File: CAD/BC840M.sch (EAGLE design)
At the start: 87 parts, among them J1 SM02B-SRSS-TB(LF)(SN), U2 BC840M, U3 LP5907MFX-3.3/NOPB, U4 LP5907MFX-3.3/NOPB, U5 ADS131M08IPBS, X1 ABM3B-8.000MHZ-B2-T, X2 FC-12M

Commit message: tweaks
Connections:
- new net VDDH: R2.2, R25.1, R28.1, R29.1, U2.A7/VDDH
- net VDD: no longer R2.2, R25.1, R28.1, R29.1, U2.A7/VDDH
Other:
- moved on the sheet: R30, R31

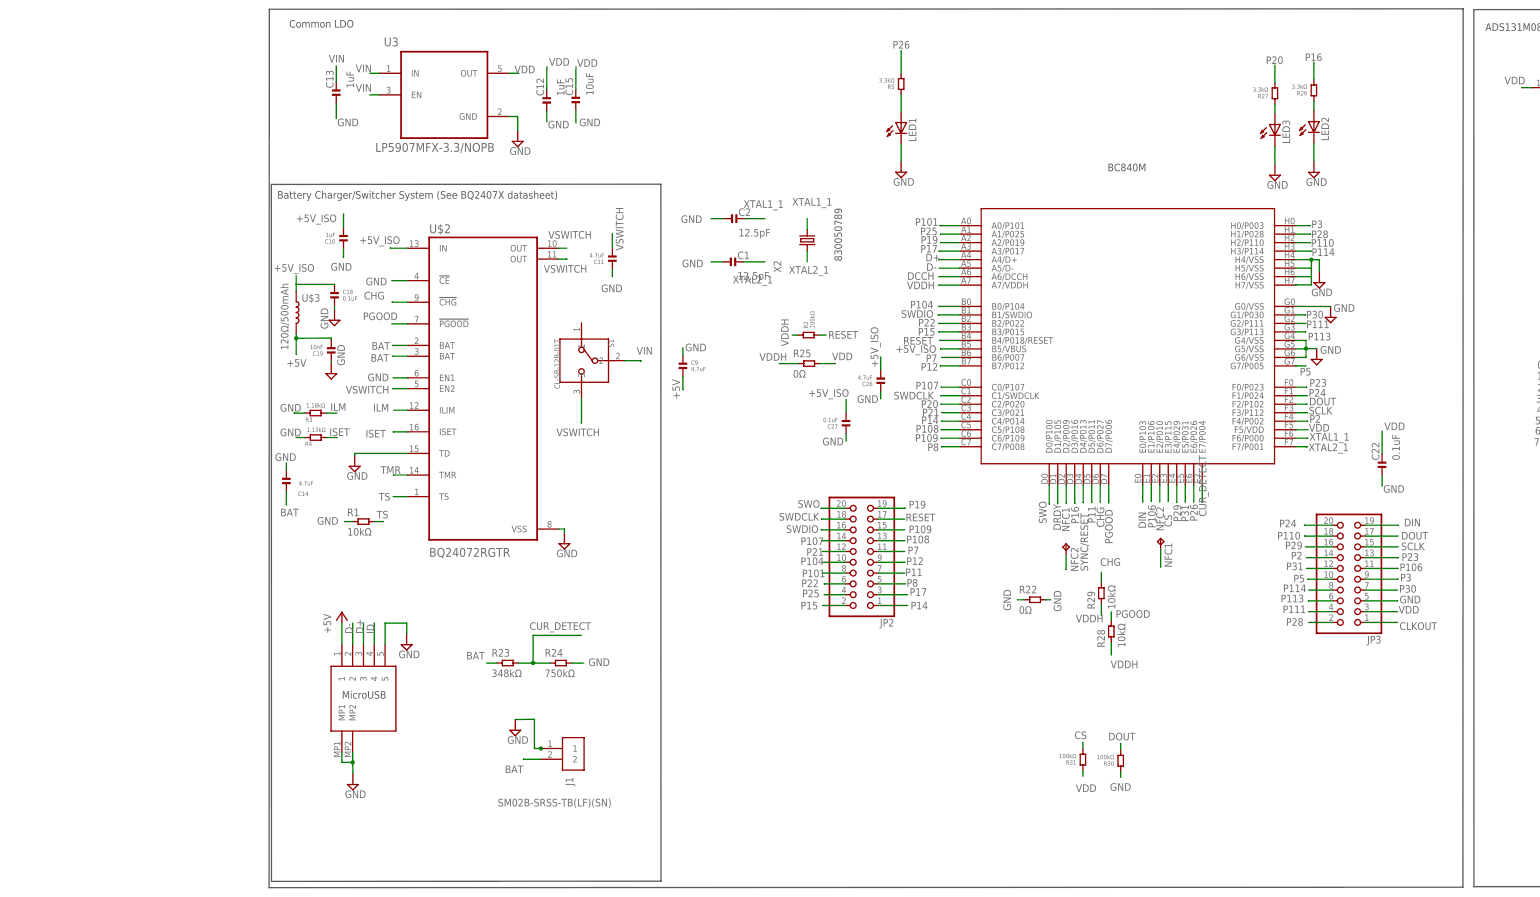
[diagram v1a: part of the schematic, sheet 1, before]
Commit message: added TVS diodes
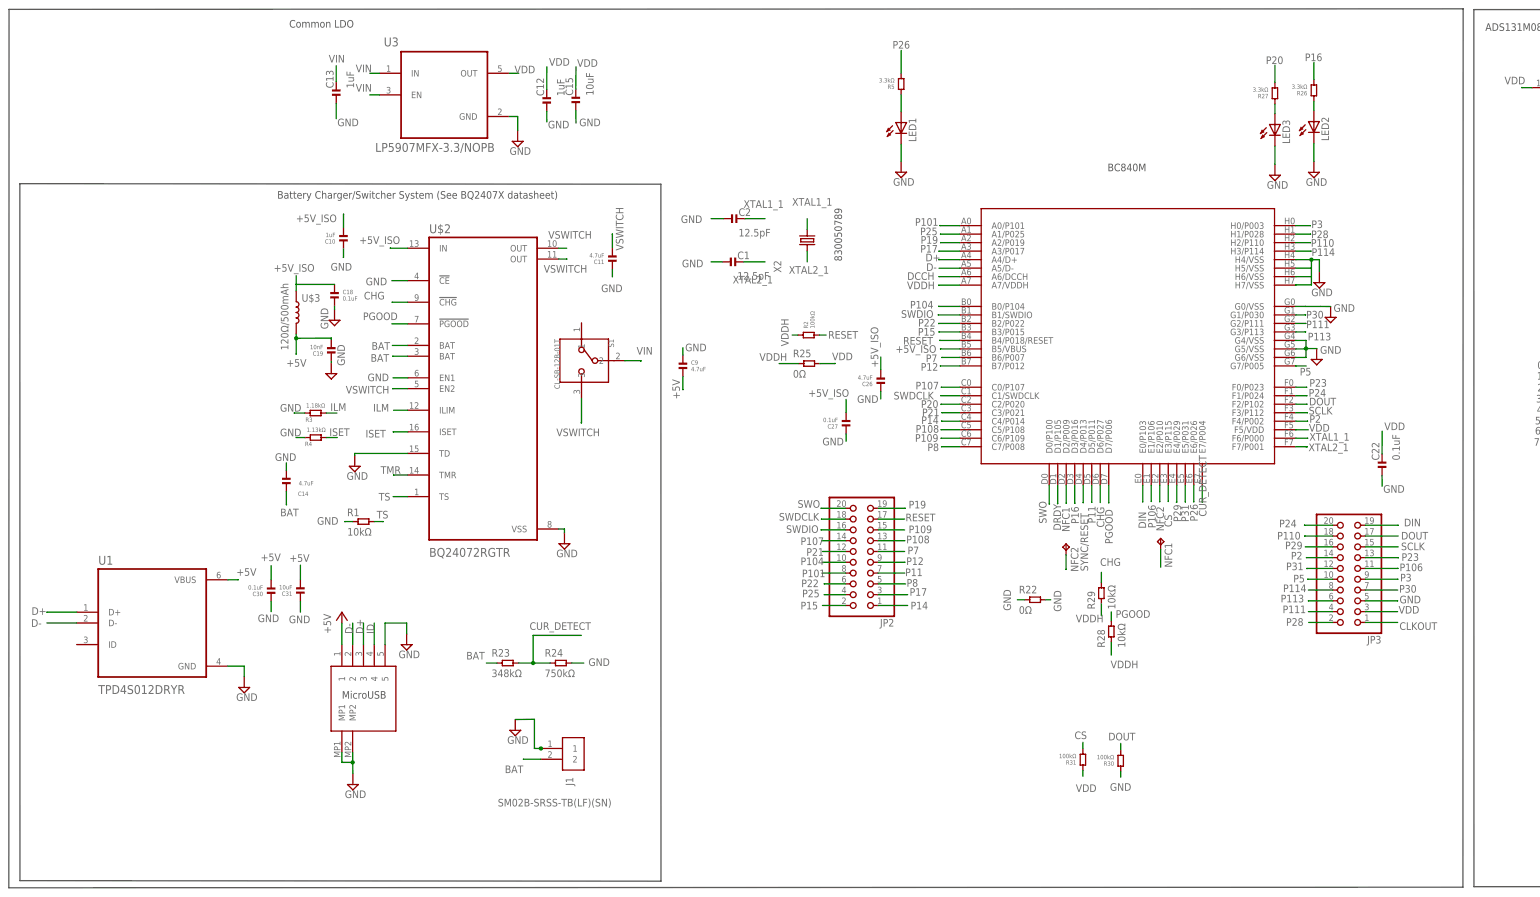
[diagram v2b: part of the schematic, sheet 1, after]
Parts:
- added C30: 0.1uF, standardparts:CAPACITOR.0201
- added C31: 10uF, standardparts:CAPACITOR.0201
- added U1: TPD4S012DRYR, TPD4S012DRYR:TPD4S012DRYR
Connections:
- net +5V: now also C30.2, C31.2, U1.VBUS
- net D+: now also U1.D+
- net D-: now also U1.D-
- net GND: now also C30.1, C31.1, U1.GND
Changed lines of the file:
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@@
 <part name="R30" library="standardparts" deviceset="RESISTOR" device=".0402" value="100kΩ"/>
 <part name="R31" library="standardparts" deviceset="RESISTOR" device=".0402" value="100kΩ"/>
+<part name="U1" library="TPD4S012DRYR" deviceset="TPD4S012DRYR" device=""/>
+<part name="SUPPLY10" library="supply2" library_urn="urn:adsk.eagle:library:372" deviceset="GND" device=""/>
+<part name="C30" library="standardparts" deviceset="CAPACITOR" device=".0201" value="0.1uF"/>
+<part name="C31" library="standardparts" deviceset="CAPACITOR" device=".0201" value="10uF"/>
 </parts>
 <sheets>
@@
 <text x="35.179" y="50.9016" size="1.778" layer="97">MicroUSB</text>
 <wire x1="110.236" y1="7.9756" x2="110.2106" y2="171.9072" width="0.1524" layer="97"/>
-<wire x1="110.2106" y1="171.9072" x2="18.5928" y2="171.8564" width="0.1524" layer="97"/>
-<wire x1="18.5928" y1="171.8564" x2="18.6182" y2="7.9248" width="0.1524" layer="97"/>
-<wire x1="18.6182" y1="7.9248" x2="110.236" y2="7.9756" width="0.1524" layer="97"/>
+<wire x1="110.2106" y1="171.9072" x2="-40.5638" y2="172.0342" width="0.1524" layer="97"/>
+<wire x1="-40.5638" y1="172.0342" x2="-40.5384" y2="8.1026" width="0.1524" layer="97"/>
+<wire x1="-40.5384" y1="8.1026" x2="110.236" y2="7.9756" width="0.1524" layer="97"/>
 <text x="19.9644" y="168.5036" size="1.778" layer="97">Battery Charger/Switcher System (See BQ2407X datasheet)</text>
 <wire x1="476.7072" y1="6.6802" x2="301.4472" y2="6.6802" width="0.1524" layer="97"/>
@@
 <wire x1="476.6818" y1="212.979" x2="476.7072" y2="6.6802" width="0.1524" layer="97"/>
 <text x="304.1142" y="207.9752" size="1.778" layer="97">ADS131M08 Circuitry</text>
-<wire x1="18.1102" y1="213.0552" x2="298.9072" y2="213.1568" width="0.1524" layer="97"/>
+<wire x1="-43.1038" y1="213.0298" x2="298.9072" y2="213.1568" width="0.1524" layer="97"/>
 <wire x1="298.9072" y1="213.1568" x2="298.8564" y2="6.5532" width="0.1524" layer="97"/>
-<wire x1="298.8564" y1="6.5532" x2="18.0594" y2="6.4516" width="0.1524" layer="97"/>
-<wire x1="18.0594" y1="6.4516" x2="18.1102" y2="213.0552" width="0.1524" layer="97"/>
+<wire x1="298.8564" y1="6.5532" x2="-43.1546" y2="6.4262" width="0.1524" layer="97"/>
+<wire x1="-43.1546" y1="6.4262" x2="-43.1038" y2="213.0298" width="0.1524" layer="97"/>
 <text x="22.7838" y="208.7372" size="1.778" layer="97">Common LDO</text>
 <text x="215.265" y="174.9552" size="1.778" layer="97">BC840M</text>
@@
 <attribute name="NAME" x="207.9244" y="35.3822" size="1.016" layer="95" rot="MR0"/>
 <attribute name="VALUE" x="207.9244" y="37.9222" size="1.016" layer="96" rot="R180"/>
+</instance>
+<instance part="U1" gate="G$1" x="-9.4234" y="68.707" smashed="yes">
+<attribute name="NAME" x="-22.1234" y="82.407" size="2.0828" layer="95" ratio="10" rot="SR0"/>
+<attribute name="VALUE" x="-22.1234" y="52.007" size="2.0828" layer="96" ratio="10" rot="SR0"/>
+</instance>
+<instance part="SUPPLY10" gate="GND" x="12.2174" y="53.5432" smashed="yes">
+<attribute name="VALUE" x="10.3124" y="50.3682" size="1.778" layer="96"/>
+</instance>
+<instance part="C30" gate="G$1" x="18.542" y="76.3016" smashed="yes" rot="R90">
+<attribute name="NAME" x="16.637" y="75.0316" size="1.016" layer="95" rot="MR0"/>
+<attribute name="VALUE" x="16.637" y="77.5716" size="1.016" layer="96" rot="R180"/>
+</instance>
+<instance part="C31" gate="G$1" x="25.4254" y="76.3524" smashed="yes" rot="R90">
+<attribute name="NAME" x="23.5204" y="75.0824" size="1.016" layer="95" rot="MR0"/>
+<attribute name="VALUE" x="23.5204" y="77.6224" size="1.016" layer="96" rot="R180"/>
 </instance>
 </instances>
@@
 <label x="215.8238" y="29.2354" size="1.778" layer="95"/>
 </segment>
+<segment>
+<pinref part="U1" gate="G$1" pin="GND"/>
+<pinref part="SUPPLY10" gate="GND" pin="GND"/>
+<wire x1="8.3566" y1="58.547" x2="12.2174" y2="58.547" width="0.1524" layer="91"/>
+<wire x1="12.2174" y1="58.547" x2="12.2174" y2="56.0832" width="0.1524" layer="91"/>
+</segment>
+<segment>
+<pinref part="C30" gate="G$1" pin="1"/>
+<wire x1="18.542" y1="73.7616" x2="18.542" y2="71.374" width="0.1524" layer="91"/>
+<label x="15.3924" y="68.9102" size="1.778" layer="95"/>
+</segment>
+<segment>
+<pinref part="C31" gate="G$1" pin="1"/>
+<wire x1="25.4254" y1="73.8124" x2="25.4254" y2="71.247" width="0.1524" layer="91"/>
+<label x="22.7076" y="68.6562" size="1.778" layer="95"/>
+</segment>
 </net>
 <net name="CLKIN" class="0">
@@
 <label x="114.681" y="121.3104" size="1.778" layer="95" rot="R90"/>
 </segment>
+<segment>
+<pinref part="U1" gate="G$1" pin="VBUS"/>
+<wire x1="8.3566" y1="78.867" x2="10.7696" y2="78.867" width="0.1524" layer="91"/>
+<wire x1="10.7696" y1="78.867" x2="10.7696" y2="78.8924" width="0.1524" layer="91"/>
+<label x="10.3632" y="79.8068" size="1.778" layer="95"/>
+</segment>
+<segment>
+<pinref part="C30" gate="G$1" pin="2"/>
+<wire x1="18.542" y1="78.8416" x2="18.542" y2="82.1944" width="0.1524" layer="91"/>
+<label x="16.0782" y="83.2612" size="1.778" layer="95"/>
+</segment>
+<segment>
+<pinref part="C31" gate="G$1" pin="2"/>
+<wire x1="25.4254" y1="78.8924" x2="25.4254" y2="82.3214" width="0.1524" layer="91"/>
+<label x="22.8346" y="83.0834" size="1.778" layer="95"/>
+</segment>
 </net>
 <net name="D-" class="0">
@@
 <label x="172.6184" y="151.511" size="1.778" layer="95"/>
 </segment>
+<segment>
+<pinref part="U1" gate="G$1" pin="D-"/>
+<wire x1="-27.2034" y1="68.707" x2="-34.1884" y2="68.707" width="0.1524" layer="91"/>
+<label x="-37.9222" y="67.7926" size="1.778" layer="95"/>
+</segment>
 </net>
 <net name="D+" class="0">
@@
 <label x="172.4406" y="153.7716" size="1.778" layer="95"/>
 </segment>
-</net>
+<segment>
+<pinref part="U1" gate="G$1" pin="D+"/>
+<wire x1="-27.2034" y1="71.247" x2="-34.1884" y2="71.247" width="0.1524" layer="91"/>
+<wire x1="-34.1884" y1="71.247" x2="-34.1884" y2="71.2216" width="0.1524" layer="91"/>
+<label x="-37.8206" y="70.612" size="1.778" layer="95"/>
+</segment>
+</net>

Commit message: push
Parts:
- C16, C17, C20, C21, C24, C25, C28, C29: value 10pF -> 100pF
- R10, R11, R12, R13, R14, R15, R16, R17, R18, R19, R20, R21, R6, R7, R8, R9: value 10MOhm -> 1MOhm
- renumbered U$1 to U7, U$2 to U6, U$3 to I1

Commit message: latest
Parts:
- C15, C31: device standardparts:CAPACITOR.0201 -> standardparts:CAPACITOR.0402
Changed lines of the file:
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@@
 <grid distance="1" unitdist="mil" unit="mil" style="lines" multiple="1" display="no" altdistance="0.01" altunitdist="inch" altunit="inch"/>
 <layers>
-<layer number="1" name="Top" color="4" fill="1" visible="no" active="no"/>
-<layer number="2" name="Route2" color="16" fill="1" visible="no" active="no"/>
-<layer number="3" name="Route3" color="17" fill="1" visible="no" active="no"/>
-<layer number="4" name="Route4" color="18" fill="1" visible="no" active="no"/>
-<layer number="5" name="Route5" color="19" fill="1" visible="no" active="no"/>
-<layer number="6" name="Route6" color="25" fill="1" visible="no" active="no"/>
-<layer number="7" name="Route7" color="26" fill="1" visible="no" active="no"/>
-<layer number="8" name="Route8" color="27" fill="1" visible="no" active="no"/>
-<layer number="9" name="Route9" color="28" fill="1" visible="no" active="no"/>
-<layer number="10" name="Route10" color="29" fill="1" visible="no" active="no"/>
-<layer number="11" name="Route11" color="30" fill="1" visible="no" active="no"/>
-<layer number="12" name="Route12" color="20" fill="1" visible="no" active="no"/>
-<layer number="13" name="Route13" color="21" fill="1" visible="no" active="no"/>
-<layer number="14" name="Route14" color="22" fill="1" visible="no" active="no"/>
-<layer number="15" name="Route15" color="23" fill="1" visible="no" active="no"/>
-<layer number="16" name="Bottom" color="1" fill="1" visible="no" active="no"/>
-<layer number="17" name="Pads" color="2" fill="1" visible="no" active="no"/>
-<layer number="18" name="Vias" color="2" fill="1" visible="no" active="no"/>
-<layer number="19" name="Unrouted" color="6" fill="1" visible="no" active="no"/>
-<layer number="20" name="Dimension" color="24" fill="1" visible="no" active="no"/>
-<layer number="21" name="tPlace" color="7" fill="1" visible="no" active="no"/>
-<layer number="22" name="bPlace" color="7" fill="1" visible="no" active="no"/>
-<layer number="23" name="tOrigins" color="15" fill="1" visible="no" active="no"/>
-<layer number="24" name="bOrigins" color="15" fill="1" visible="no" active="no"/>
-<layer number="25" name="tNames" color="7" fill="1" visible="no" active="no"/>
-<layer number="26" name="bNames" color="7" fill="1" visible="no" active="no"/>
-<layer number="27" name="tValues" color="7" fill="1" visible="no" active="no"/>
-<layer number="28" name="bValues" color="7" fill="1" visible="no" active="no"/>
+<layer number="1" name="Top" color="4" fill="1" visible="yes" active="no"/>
+<layer number="2" name="Route2" color="16" fill="1" visible="yes" active="no"/>
+<layer number="3" name="Route3" color="17" fill="1" visible="yes" active="no"/>
+<layer number="4" name="Route4" color="18" fill="1" visible="yes" active="no"/>
+<layer number="5" name="Route5" color="19" fill="1" visible="yes" active="no"/>
+<layer number="6" name="Route6" color="25" fill="1" visible="yes" active="no"/>
+<layer number="7" name="Route7" color="26" fill="1" visible="yes" active="no"/>
+<layer number="8" name="Route8" color="27" fill="1" visible="yes" active="no"/>
+<layer number="9" name="Route9" color="28" fill="1" visible="yes" active="no"/>
+<layer number="10" name="Route10" color="29" fill="1" visible="yes" active="no"/>
+<layer number="11" name="Route11" color="30" fill="1" visible="yes" active="no"/>
+<layer number="12" name="Route12" color="20" fill="1" visible="yes" active="no"/>
+<layer number="13" name="Route13" color="21" fill="1" visible="yes" active="no"/>
+<layer number="14" name="Route14" color="22" fill="1" visible="yes" active="no"/>
+<layer number="15" name="Route15" color="23" fill="1" visible="yes" active="no"/>
+<layer number="16" name="Bottom" color="1" fill="1" visible="yes" active="no"/>
+<layer number="17" name="Pads" color="2" fill="1" visible="yes" active="no"/>
+<layer number="18" name="Vias" color="2" fill="1" visible="yes" active="no"/>
+<layer number="19" name="Unrouted" color="6" fill="1" visible="yes" active="no"/>
+<layer number="20" name="Dimension" color="24" fill="1" visible="yes" active="no"/>
+<layer number="21" name="tPlace" color="7" fill="1" visible="yes" active="no"/>
+<layer number="22" name="bPlace" color="7" fill="1" visible="yes" active="no"/>
+<layer number="23" name="tOrigins" color="15" fill="1" visible="yes" active="no"/>
+<layer number="24" name="bOrigins" color="15" fill="1" visible="yes" active="no"/>
+<layer number="25" name="tNames" color="7" fill="1" visible="yes" active="no"/>
+<layer number="26" name="bNames" color="7" fill="1" visible="yes" active="no"/>
+<layer number="27" name="tValues" color="7" fill="1" visible="yes" active="no"/>
+<layer number="28" name="bValues" color="7" fill="1" visible="yes" active="no"/>
 <layer number="29" name="tStop" color="7" fill="3" visible="no" active="no"/>
 <layer number="30" name="bStop" color="7" fill="6" visible="no" active="no"/>
@@
 <layer number="35" name="tGlue" color="7" fill="4" visible="no" active="no"/>
 <layer number="36" name="bGlue" color="7" fill="5" visible="no" active="no"/>
-<layer number="37" name="tTest" color="7" fill="1" visible="no" active="no"/>
-<layer number="38" name="bTest" color="7" fill="1" visible="no" active="no"/>
+<layer number="37" name="tTest" color="7" fill="1" visible="yes" active="no"/>
+<layer number="38" name="bTest" color="7" fill="1" visible="yes" active="no"/>
 <layer number="39" name="tKeepout" color="4" fill="11" visible="no" active="no"/>
 <layer number="40" name="bKeepout" color="1" fill="11" visible="no" active="no"/>
@@
 <layer number="44" name="Drills" color="7" fill="1" visible="no" active="no"/>
 <layer number="45" name="Holes" color="7" fill="1" visible="no" active="no"/>
-<layer number="46" name="Milling" color="3" fill="1" visible="no" active="no"/>
-<layer number="47" name="Measures" color="7" fill="1" visible="no" active="no"/>
-<layer number="48" name="Document" color="7" fill="1" visible="no" active="no"/>
-<layer number="49" name="Reference" color="7" fill="1" visible="no" active="no"/>
-<layer number="50" name="dxf" color="7" fill="1" visible="no" active="no"/>
-<layer number="51" name="tDocu" color="7" fill="1" visible="no" active="no"/>
-<layer number="52" name="bDocu" color="7" fill="1" visible="no" active="no"/>
-<layer number="53" name="tGND_GNDA" color="7" fill="9" visible="no" active="no"/>
-<layer number="54" name="bGND_GNDA" color="1" fill="9" visible="no" active="no"/>
-<layer number="56" name="wert" color="7" fill="1" visible="no" active="no"/>
-<layer number="57" name="tCAD" color="7" fill="1" visible="no" active="no"/>
-<layer number="58" name="bCAD" color="7" fill="1" visible="no" active="no"/>
-<layer number="59" name="tCarbon" color="7" fill="1" visible="no" active="no"/>
-<layer number="60" name="bCarbon" color="7" fill="1" visible="no" active="no"/>
+<layer number="46" name="Milling" color="3" fill="1" visible="yes" active="no"/>
+<layer number="47" name="Measures" color="7" fill="1" visible="yes" active="no"/>
+<layer number="48" name="Document" color="7" fill="1" visible="yes" active="no"/>
+<layer number="49" name="Reference" color="7" fill="1" visible="yes" active="no"/>
+<layer number="50" name="dxf" color="7" fill="1" visible="yes" active="no"/>
+<layer number="51" name="tDocu" color="7" fill="1" visible="yes" active="no"/>
+<layer number="52" name="bDocu" color="7" fill="1" visible="yes" active="no"/>
+<layer number="53" name="tGND_GNDA" color="7" fill="9" visible="yes" active="no"/>
+<layer number="54" name="bGND_GNDA" color="1" fill="9" visible="yes" active="no"/>
+<layer number="56" name="wert" color="7" fill="1" visible="yes" active="no"/>
+<layer number="57" name="tCAD" color="7" fill="1" visible="yes" active="no"/>
+<layer number="58" name="bCAD" color="7" fill="1" visible="yes" active="no"/>
+<layer number="59" name="tCarbon" color="7" fill="1" visible="yes" active="no"/>
+<layer number="60" name="bCarbon" color="7" fill="1" visible="yes" active="no"/>
 <layer number="88" name="SimResults" color="9" fill="1" visible="yes" active="yes"/>
 <layer number="89" name="SimProbes" color="9" fill="1" visible="yes" active="yes"/>
@@
 <part name="SUPPLY7" library="supply2" library_urn="urn:adsk.eagle:library:372" deviceset="GND" device=""/>
 <part name="SUPPLY11" library="supply2" library_urn="urn:adsk.eagle:library:372" deviceset="GND" device=""/>
-<part name="C15" library="standardparts" deviceset="CAPACITOR" device=".0201" value="10uF"/>
+<part name="C15" library="standardparts" deviceset="CAPACITOR" device=".0402" value="10uF"/>
 <part name="SUPPLY13" library="supply2" library_urn="urn:adsk.eagle:library:372" deviceset="GND" device=""/>
 <part name="U2" library="BC840M" deviceset="BC840M" device=""/>
@@
 <part name="SUPPLY10" library="supply2" library_urn="urn:adsk.eagle:library:372" deviceset="GND" device=""/>
 <part name="C30" library="standardparts" deviceset="CAPACITOR" device=".0201" value="0.1uF"/>
-<part name="C31" library="standardparts" deviceset="CAPACITOR" device=".0201" value="10uF"/>
+<part name="C31" library="standardparts" deviceset="CAPACITOR" device=".0402" value="10uF"/>
 </parts>
 <sheets>

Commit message: edits and CAM
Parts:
- J1: value SM02B-SRSS-TB(LF)(SN) -> S2B-PH-SM4-TB(LF)(SN); device SM02B-SRSS-TB_LF__SN_:SM02B-SRSS-TB(LF)(SN) -> S2B-PH-SM4-TB_LF__SN_:S2B-PH-SM4-TB(LF)(SN)
